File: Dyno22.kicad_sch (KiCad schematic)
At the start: 49 parts, among them J2 Display, J3 Pwr Output, J4 BPM & Sensors, J5 Pwr Input, J7 UART, SW1 SW_DPST_x2, U1 TS2937CW50, U2 LM324, U3 Demux

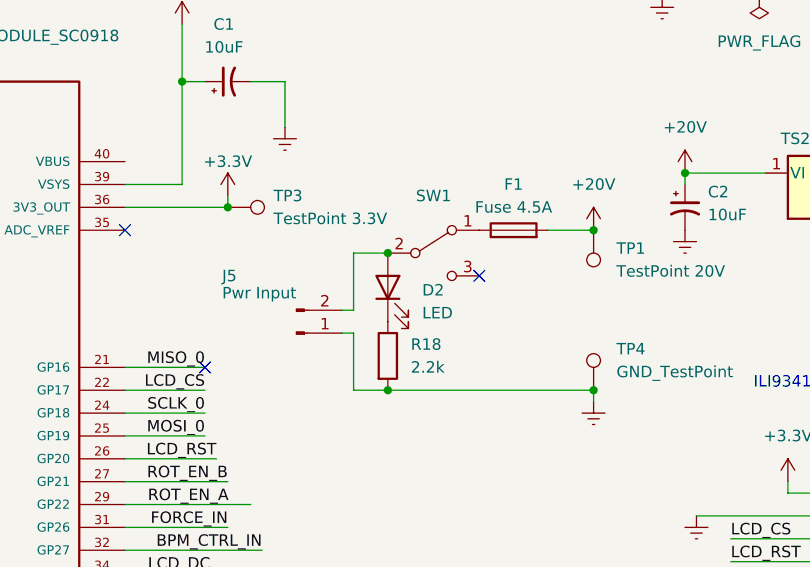
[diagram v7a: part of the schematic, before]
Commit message: moved components and fixed connections to accomodate for new pico location and power components
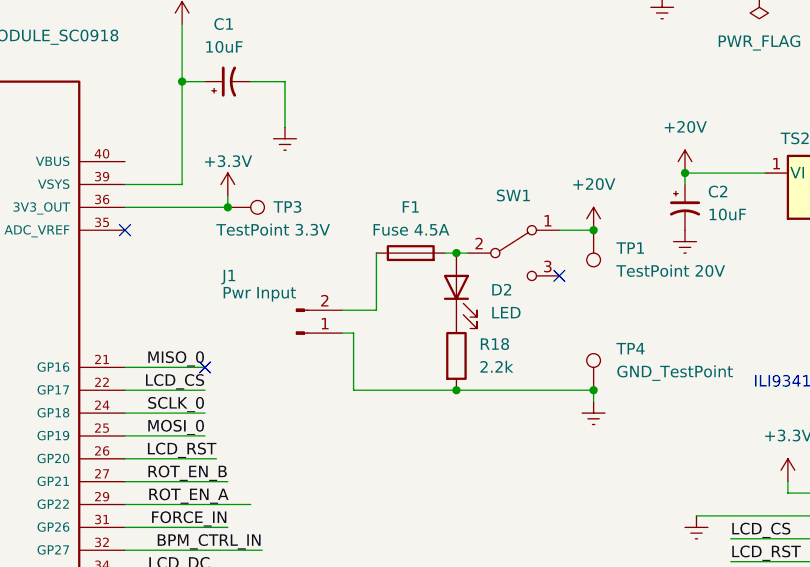
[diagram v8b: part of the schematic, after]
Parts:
- TP4: footprint TestPoint:TestPoint_Pad_4.0x4.0mm -> TestPoint:TestPoint_Loop_D2.60mm_Drill1.4mm_Beaded
- renumbered J5 to J1
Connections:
- net +24V: now also SW1.1 (A); no longer F1.2
- net at F1.1: now also J1.2 (Pin_2); no longer SW1.1 (A)
- net at D2.2 (A), SW1.2 (B): now also F1.2; no longer J1.2 (Pin_2)
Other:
- moved on the sheet: D2, F1, R18, SW1
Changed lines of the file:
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@@
 (kicad_sch (version 20230121) (generator eeschema)
   (paper "A4")
-  (junction (at 110.49 48.26) (diameter 0) (color 0 0 0 0)
-  )
-  (junction (at 110.49 63.5) (diameter 0) (color 0 0 0 0)
-  )
   (junction (at 105.41 151.13) (diameter 0) (color 0 0 0 0)
   )
+  (junction (at 118.11 63.5) (diameter 0) (color 0 0 0 0)
+  )
   (junction (at 176.53 27.94) (diameter 0) (color 0 0 0 0)
   )
@@
   (junction (at 225.425 108.585) (diameter 0) (color 0 0 0 0)
   )
+  (junction (at 118.11 48.26) (diameter 0) (color 0 0 0 0)
+  )
   (junction (at 26.67 101.6) (diameter 0) (color 0 0 0 0)
   )
@@
   (no_connect (at 30.48 38.1))
   (no_connect (at 160.02 95.25))
-  (no_connect (at 120.65 50.8))
+  (no_connect (at 129.54 50.8))
   (no_connect (at 63.5 132.08))
   (no_connect (at 105.41 104.14))
@@
     (stroke (width 0) (type default))
   )
+  (wire (pts (xy 129.54 45.72) (xy 133.35 45.72))
+    (stroke (width 0) (type default))
+  )
   (wire (pts (xy 212.725 94.615) (xy 212.725 103.505))
     (stroke (width 0) (type default))
@@
     (stroke (width 0) (type default))
   )
-  (wire (pts (xy 128.27 45.72) (xy 133.35 45.72))
+  (wire (pts (xy 116.84 48.26) (xy 118.11 48.26))
     (stroke (width 0) (type default))
   )
@@
     (stroke (width 0) (type default))
   )
+  (wire (pts (xy 118.11 48.26) (xy 119.38 48.26))
+    (stroke (width 0) (type default))
+  )
+  (wire (pts (xy 118.11 63.5) (xy 133.35 63.5))
+    (stroke (width 0) (type default))
+  )
   (wire (pts (xy 100.33 116.84) (xy 105.41 116.84))
     (stroke (width 0) (type default))
   )
-  (wire (pts (xy 110.49 63.5) (xy 133.35 63.5))
+  (wire (pts (xy 106.68 63.5) (xy 118.11 63.5))
     (stroke (width 0) (type default))
   )
@@
     (stroke (width 0) (type default))
   )
-  (wire (pts (xy 106.68 54.61) (xy 106.68 48.26))
+  (wire (pts (xy 109.22 54.61) (xy 109.22 48.26))
     (stroke (width 0) (type default))
   )
@@
     (stroke (width 0) (type default))
   )
-  (wire (pts (xy 106.68 48.26) (xy 110.49 48.26))
-    (stroke (width 0) (type default))
-  )
   (wire (pts (xy 260.985 88.265) (xy 272.415 88.265))
     (stroke (width 0) (type default))
@@
     (stroke (width 0) (type default))
   )
-  (wire (pts (xy 106.68 63.5) (xy 110.49 63.5))
-    (stroke (width 0) (type default))
-  )
   (wire (pts (xy 30.48 104.14) (xy 26.67 104.14))
     (stroke (width 0) (type default))
@@
     (stroke (width 0) (type default))
   )
-  (wire (pts (xy 105.41 54.61) (xy 106.68 54.61))
+  (wire (pts (xy 105.41 54.61) (xy 109.22 54.61))
     (stroke (width 0) (type default))
   )
@@
     )
   )
-  (symbol (lib_id "Switch:SW_SPDT") (at 115.57 48.26 0) (unit 1)
+  (symbol (lib_id "Switch:SW_SPDT") (at 124.46 48.26 0) (unit 1)
     (in_bom yes) (on_board yes) (dnp no) (fields_autoplaced)
-    (property "Reference" "SW1" (at 115.57 41.91 0)
+    (property "Reference" "SW1" (at 124.46 41.91 0)
       (effects (font (size 1.27 1.27)))
     )
-    (property "Value" "SW_DPST_x2" (at 115.57 44.45 0)
+    (property "Value" "SW_DPST_x2" (at 124.46 44.45 0)
       (effects (font (size 1.27 1.27)) hide)
     )
-    (property "Footprint" "300SP1J1BLKM2QE:SW_300SP1J1BLKM2QE" (at 115.57 48.26 0)
+    (property "Footprint" "300SP1J1BLKM2QE:SW_300SP1J1BLKM2QE" (at 124.46 48.26 0)
       (effects (font (size 1.27 1.27)) hide)
     )
-    (property "Datasheet" "~" (at 115.57 48.26 0)
+    (property "Datasheet" "~" (at 124.46 48.26 0)
       (effects (font (size 1.27 1.27)) hide)
     )
@@
   (symbol (lib_id "Connector:Conn_01x02_Male") (at 100.33 57.15 0) (mirror x) (unit 1)
     (in_bom yes) (on_board yes) (dnp no)
-    (property "Reference" "J5" (at 92.075 50.8 0)
+    (property "Reference" "J1" (at 92.075 50.8 0)
       (effects (font (size 1.27 1.27)) (justify left))
     )
@@
       (project "Dyno22"
         (path "/7271225a-6695-4332-8687-d26f1f45d708"
-          (reference "J5") (unit 1)
+          (reference "J1") (unit 1)
         )
       )
@@
   )
   (symbol (lib_id "Connector:TestPoint") (at 92.71 43.18 270) (unit 1)
-    (in_bom yes) (on_board yes) (dnp no) (fields_autoplaced)
-    (property "Reference" "TP3" (at 97.79 41.91 90)
+    (in_bom yes) (on_board yes) (dnp no)
+    (property "Reference" "TP3" (at 97.79 43.18 90)
       (effects (font (size 1.27 1.27)) (justify left))
     )
-    (property "Value" "TestPoint 3.3V" (at 97.79 44.45 90)
+    (property "Value" "TestPoint 3.3V" (at 91.44 45.72 90)
       (effects (font (size 1.27 1.27)) (justify left))
     )
@@
     )
   )
-  (symbol (lib_id "Device:LED") (at 110.49 52.07 90) (unit 1)
+  (symbol (lib_id "Device:LED") (at 118.11 52.07 90) (unit 1)
     (in_bom yes) (on_board yes) (dnp no) (fields_autoplaced)
-    (property "Reference" "D2" (at 114.3 52.3875 90)
+    (property "Reference" "D2" (at 121.92 52.3875 90)
       (effects (font (size 1.27 1.27)) (justify right))
     )
-    (property "Value" "LED" (at 114.3 54.9275 90)
+    (property "Value" "LED" (at 121.92 54.9275 90)
       (effects (font (size 1.27 1.27)) (justify right))
     )
-    (property "Footprint" "LED_SMD:LED_0603_1608Metric" (at 110.49 52.07 0)
+    (property "Footprint" "LED_SMD:LED_0603_1608Metric" (at 118.11 52.07 0)
       (effects (font (size 1.27 1.27)) hide)
     )
-    (property "Datasheet" "https://www.digikey.ca/en/products/detail/liteon/LTST-C191KRKT/386837" (at 110.49 52.07 0)
+    (property "Datasheet" "https://www.digikey.ca/en/products/detail/liteon/LTST-C191KRKT/386837" (at 118.11 52.07 0)
       (effects (font (size 1.27 1.27)) hide)
     )
@@
     )
   )
-  (symbol (lib_id "Device:Fuse") (at 124.46 45.72 90) (unit 1)
+  (symbol (lib_id "Device:Fuse") (at 113.03 48.26 90) (unit 1)
     (in_bom yes) (on_board yes) (dnp no) (fields_autoplaced)
-    (property "Reference" "F1" (at 124.46 40.64 90)
+    (property "Reference" "F1" (at 113.03 43.18 90)
       (effects (font (size 1.27 1.27)))
     )
-    (property "Value" "Fuse 4.5A" (at 124.46 43.18 90)
+    (property "Value" "Fuse 4.5A" (at 113.03 45.72 90)
       (effects (font (size 1.27 1.27)))
     )
-    (property "Footprint" "Fuse:Fuse_1206_3216Metric" (at 124.46 47.498 90)
+    (property "Footprint" "Fuse:Fuse_1206_3216Metric" (at 113.03 50.038 90)
       (effects (font (size 1.27 1.27)) hide)
     )
-    (property "Datasheet" "https://www.digikey.ca/en/products/detail/eaton-electronics-division/CC12H4-5A-TR/2138898" (at 124.46 45.72 0)
+    (property "Datasheet" "https://www.digikey.ca/en/products/detail/eaton-electronics-division/CC12H4-5A-TR/2138898" (at 113.03 48.26 0)
       (effects (font (size 1.27 1.27)) hide)
     )
@@
       (effects (font (size 1.27 1.27)) (justify left))
     )
-    (property "Footprint" "TestPoint:TestPoint_Pad_4.0x4.0mm" (at 138.43 63.5 0)
+    (property "Footprint" "TestPoint:TestPoint_Loop_D2.60mm_Drill1.4mm_Beaded" (at 138.43 63.5 0)
       (effects (font (size 1.27 1.27)) hide)
     )
@@
     )
   )
-  (symbol (lib_id "Device:R") (at 110.49 59.69 0) (unit 1)
+  (symbol (lib_id "Device:R") (at 118.11 59.69 0) (unit 1)
     (in_bom yes) (on_board yes) (dnp no) (fields_autoplaced)
-    (property "Reference" "R18" (at 113.03 58.42 0)
+    (property "Reference" "R18" (at 120.65 58.42 0)
       (effects (font (size 1.27 1.27)) (justify left))
     )
-    (property "Value" "2.2k" (at 113.03 60.96 0)
+    (property "Value" "2.2k" (at 120.65 60.96 0)
       (effects (font (size 1.27 1.27)) (justify left))
     )
-    (property "Footprint" "Resistor_SMD:R_0402_1005Metric" (at 108.712 59.69 90)
+    (property "Footprint" "Resistor_SMD:R_0402_1005Metric" (at 116.332 59.69 90)
       (effects (font (size 1.27 1.27)) hide)
     )
-    (property "Datasheet" "https://www.digikey.ca/en/products/detail/yageo/RC0402FR-072K2L/726553" (at 110.49 59.69 0)
+    (property "Datasheet" "https://www.digikey.ca/en/products/detail/yageo/RC0402FR-072K2L/726553" (at 118.11 59.69 0)
       (effects (font (size 1.27 1.27)) hide)
     )
